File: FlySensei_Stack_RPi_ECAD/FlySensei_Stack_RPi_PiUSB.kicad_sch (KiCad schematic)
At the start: 11 parts, among them J2 USB_C_Receptacle_USB2.0, SW2 SW_SPDT, U5 TPD2EUSB30, U6 TUSB321

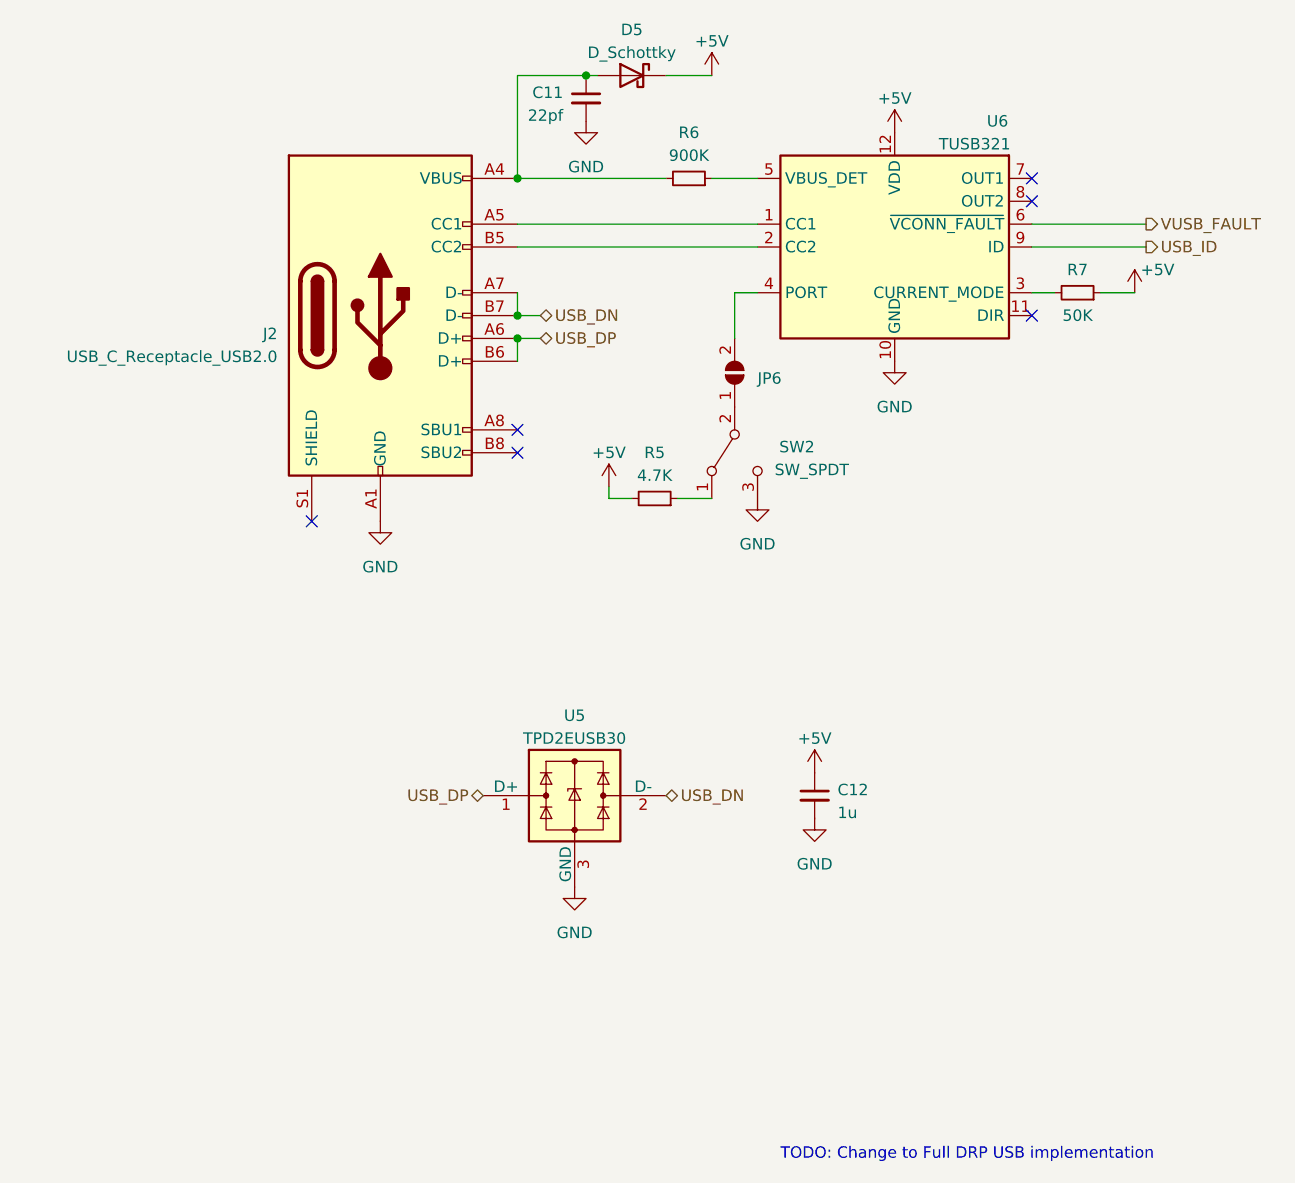
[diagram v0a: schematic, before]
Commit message: PCB Design for the Raspberry PI CM4 Board (V0.1)
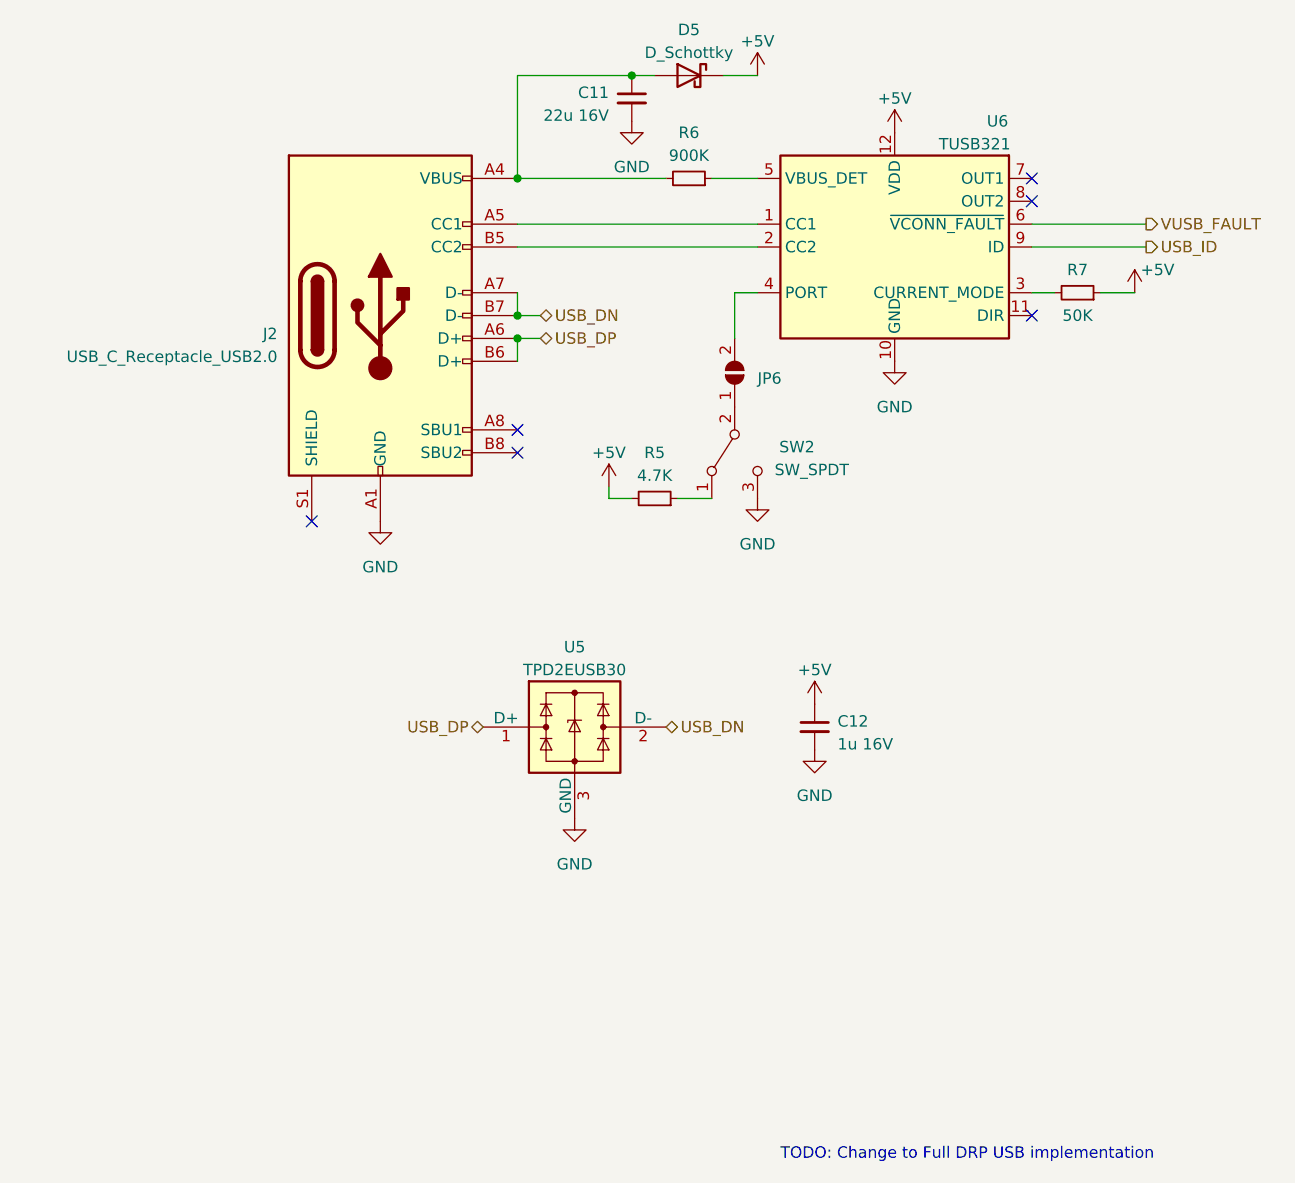
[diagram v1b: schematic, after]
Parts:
- C11: value 22pf -> 22u 16V; footprint (none) -> Capacitor_SMD:C_0603_1608Metric
- C12: value 1u -> 1u 16V; footprint (none) -> Capacitor_SMD:C_0603_1608Metric
- D5: footprint (none) -> Diode_SMD:D_SMB
- J2: footprint (none) -> Connector_USB:USB_C_Receptacle_XKB_U262-16XN-4BVC11
- JP6: footprint (none) -> Jumper:SolderJumper-2_P1.3mm_Open_RoundedPad1.0x1.5mm
- R5, R6, R7: footprint (none) -> Resistor_SMD:R_0402_1005Metric
- SW2: footprint (none) -> Button_Switch_SMD:SW_SPDT_PCM12
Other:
- moved on the sheet: C11, C12, D5, U5
